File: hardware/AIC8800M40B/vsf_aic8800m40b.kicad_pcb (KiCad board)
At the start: 4 copper layers, 36.8 x 57.2 mm, 86 parts, among them J1 USB_A, J2 USB_C_Receptacle_USB2.0, J3 USB_C_Receptacle_USB2.0, J4 Micro_SD_Card_Det1, J6 Conn_Coaxial, J7 Conn_Coaxial, J8 Conn_02x15_Odd_Even, Q1 S9013, SW1 SW_Push, SW2 SW_Push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

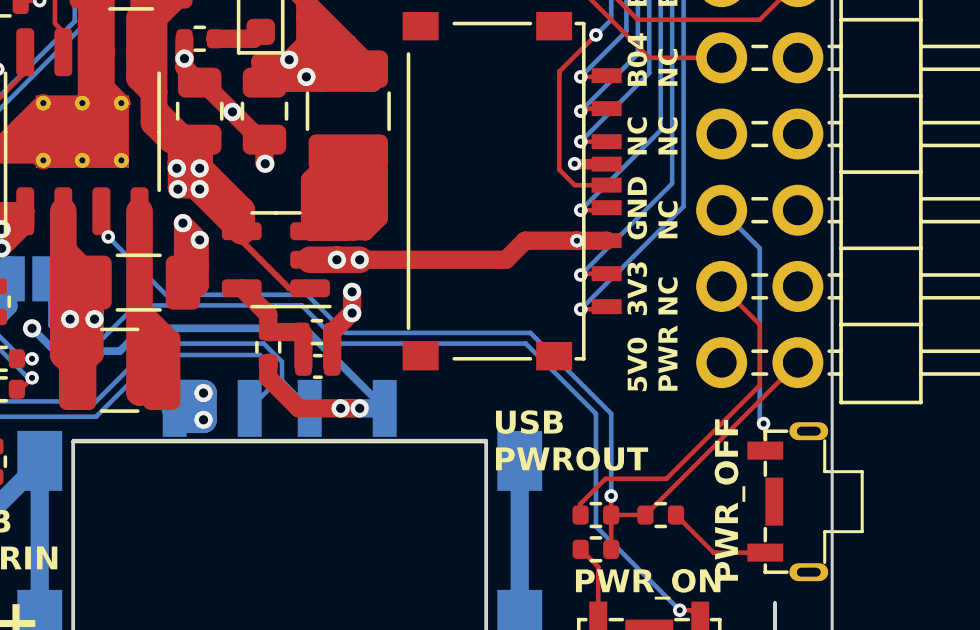
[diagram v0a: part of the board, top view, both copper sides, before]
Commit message: [hardware/aic8800m40b] connect usb signals to pin header
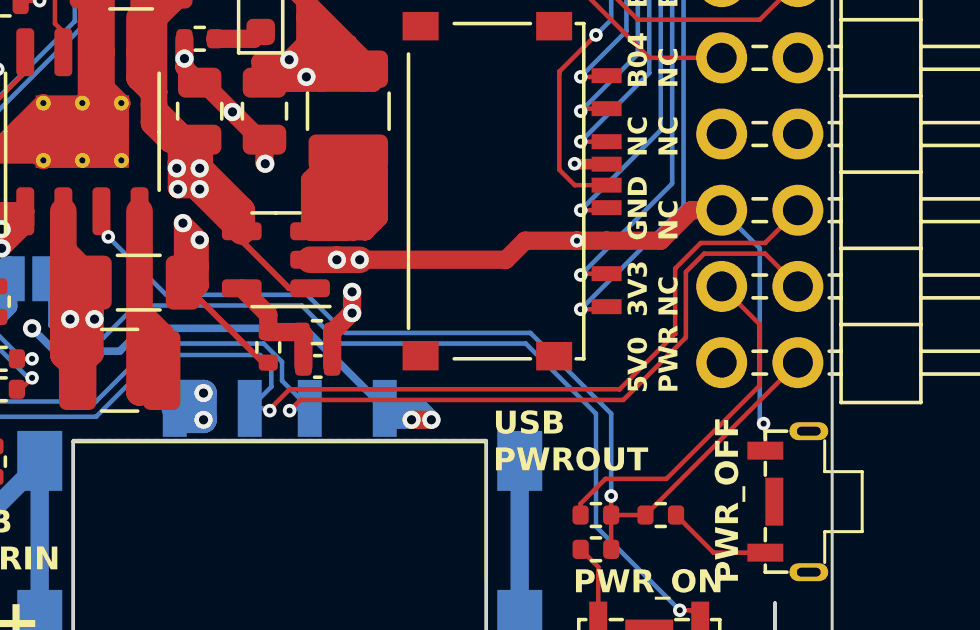
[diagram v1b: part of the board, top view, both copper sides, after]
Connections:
- J8 pad 26: unconnected-(J8-Pin_26-Pad26) -> /_USB_DM
- J8 pad 28: unconnected-(J8-Pin_28-Pad28) -> /_USB_DP
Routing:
- net /_USB_DM: track 18.3 -> 40.7 mm, vias 2 -> 3
- net /_USB_DP: track 18.2 -> 39.7 mm, vias 2 -> 3
- net GND: track 332.8 -> 342.2 mm

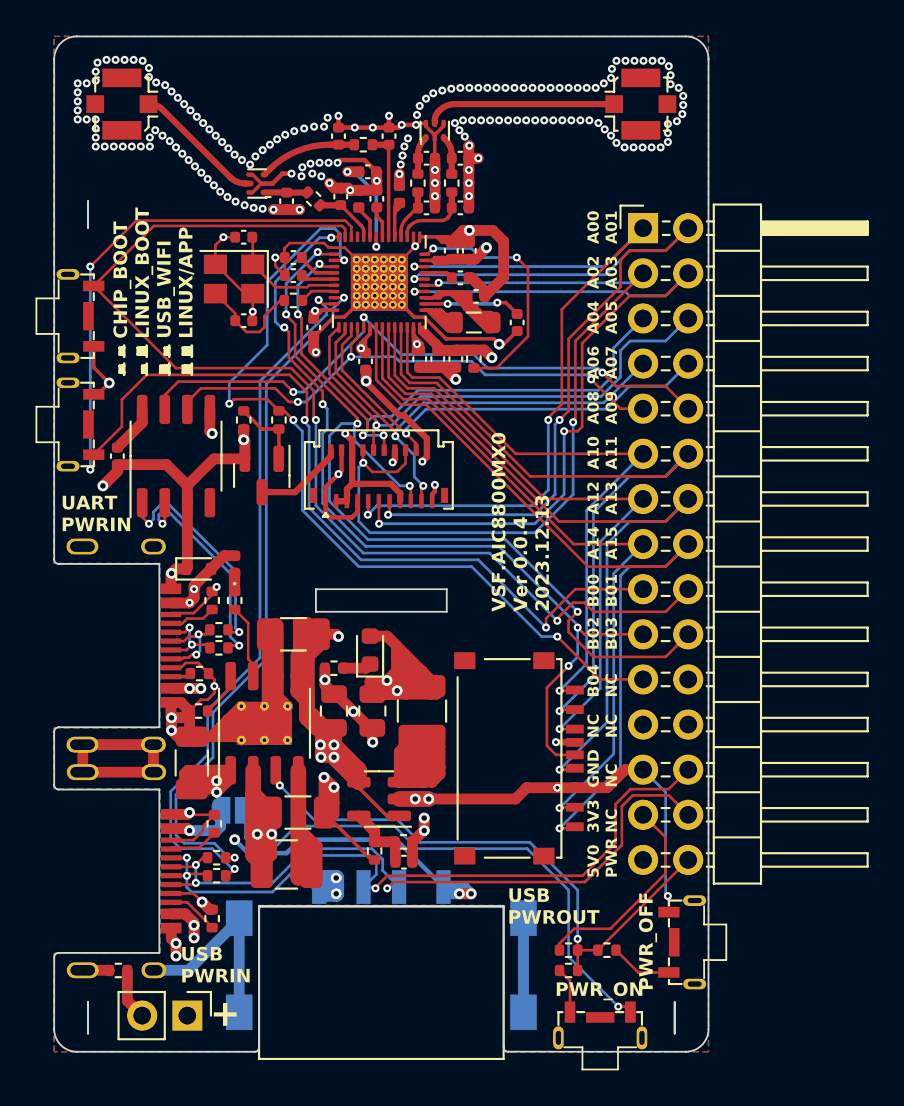
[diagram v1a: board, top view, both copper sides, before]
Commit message: [hardware/aic8800m40b] update silks
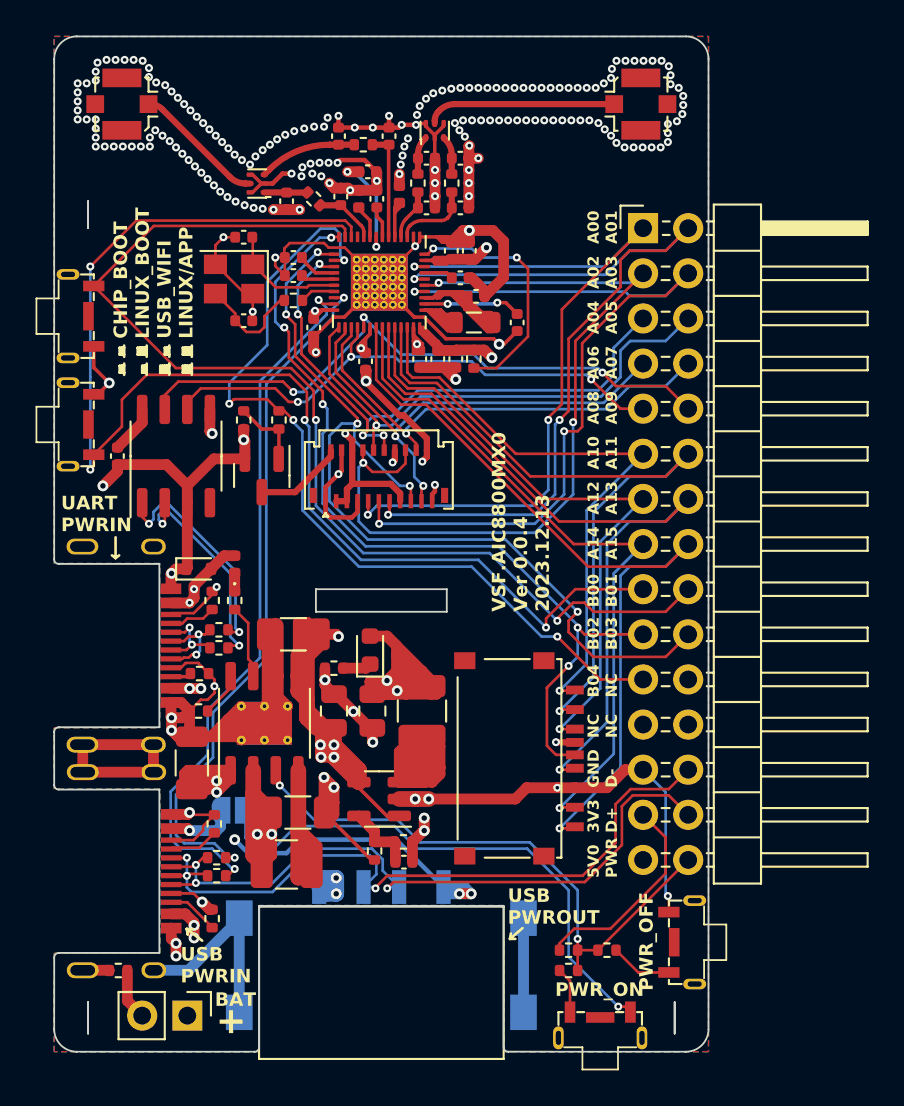
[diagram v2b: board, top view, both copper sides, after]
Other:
- board text added: "3V3 D+"
- board text added: "GND D-"
- board text removed: "3V3 NC"
- board text removed: "GND NC"
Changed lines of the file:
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@@
   (gr_line (start 206.883 112.776) (end 207.01 112.776)
     (stroke (width 0.15) (type default)) (layer "F.SilkS"))
+  (gr_line (start 211.5312 146.1516) (end 210.6676 145.4912)
+    (stroke (width 0.15) (type default)) (layer "F.SilkS"))
   (gr_line (start 209.169 114.173) (end 209.169 113.792)
     (stroke (width 0.15) (type default)) (layer "F.SilkS"))
@@
   (gr_line (start 208.407 113.157) (end 208.28 113.157)
     (stroke (width 0.15) (type default)) (layer "F.SilkS"))
+  (gr_line (start 210.6676 145.4912) (end 211.0232 145.4912)
+    (stroke (width 0.15) (type default)) (layer "F.SilkS"))
   (gr_line (start 208.28 113.792) (end 208.407 113.792)
     (stroke (width 0.15) (type default)) (layer "F.SilkS"))
@@
   (gr_line (start 210.566 112.776) (end 210.566 113.157)
     (stroke (width 0.15) (type default)) (layer "F.SilkS"))
+  (gr_line (start 210.7184 145.796) (end 210.6676 145.4912)
+    (stroke (width 0.15) (type default)) (layer "F.SilkS"))
   (gr_line (start 207.137 112.649) (end 207.137 113.284)
     (stroke (width 0.15) (type default)) (layer "F.SilkS"))
+  (gr_line (start 210.6676 145.4912) (end 210.7184 145.796)
+    (stroke (width 0.15) (type default)) (layer "F.SilkS"))
   (gr_line (start 207.899 112.776) (end 207.899 113.157)
     (stroke (width 0.15) (type default)) (layer "F.SilkS"))
@@
   (gr_line (start 210.566 113.792) (end 210.693 113.792)
     (stroke (width 0.15) (type default)) (layer "F.SilkS"))
+  (gr_line (start 206.6544 124.6124) (end 206.8576 124.46)
+    (stroke (width 0.15) (type default)) (layer "F.SilkS"))
   (gr_line (start 209.169 113.792) (end 209.296 113.792)
     (stroke (width 0.15) (type default)) (layer "F.SilkS"))
@@
   (gr_line (start 209.423 112.776) (end 209.55 112.776)
     (stroke (width 0.15) (type default)) (layer "F.SilkS"))
+  (gr_line (start 229.5652 145.4404) (end 228.854 146.05)
+    (stroke (width 0.15) (type default)) (layer "F.SilkS"))
   (gr_line (start 210.693 113.792) (end 210.693 114.173)
     (stroke (width 0.15) (type default)) (layer "F.SilkS"))
@@
   (gr_line (start 206.883 114.173) (end 207.01 114.173)
     (stroke (width 0.15) (type default)) (layer "F.SilkS"))
+  (gr_line (start 206.6544 124.6124) (end 206.4512 124.46)
+    (stroke (width 0.15) (type default)) (layer "F.SilkS"))
   (gr_line (start 207.01 113.792) (end 207.01 114.173)
     (stroke (width 0.15) (type default)) (layer "F.SilkS"))
@@
   (gr_line (start 209.423 114.173) (end 209.55 114.173)
     (stroke (width 0.15) (type default)) (layer "F.SilkS"))
+  (gr_line (start 228.854 146.05) (end 228.9048 145.7452)
+    (stroke (width 0.15) (type default)) (layer "F.SilkS"))
   (gr_line (start 209.55 113.792) (end 209.55 114.173)
     (stroke (width 0.15) (type default)) (layer "F.SilkS"))
@@
   (gr_line (start 207.137 113.665) (end 207.137 114.3)
     (stroke (width 0.15) (type default)) (layer "F.SilkS"))
+  (gr_line (start 228.854 146.05) (end 229.1588 146.05)
+    (stroke (width 0.15) (type default)) (layer "F.SilkS"))
   (gr_line (start 208.407 112.649) (end 208.407 113.284)
     (stroke (width 0.15) (type default)) (layer "F.SilkS"))
@@
     (stroke (width 0.15) (type default)) (layer "F.SilkS"))
   (gr_line (start 208.28 114.173) (end 208.28 113.792)
+    (stroke (width 0.15) (type default)) (layer "F.SilkS"))
+  (gr_line (start 206.6544 123.444) (end 206.6544 124.6124)
     (stroke (width 0.15) (type default)) (layer "F.SilkS"))
   (gr_line (start 209.55 113.792) (end 209.423 113.792)
@@
     (effects (font (size 0.762 0.762) (thickness 0.1524) bold) (justify left bottom))
   )
-  (gr_text "GND\nNC" (at 234.95 137.541 90) (layer "F.SilkS")
-    (effects (font (size 0.635 0.635) (thickness 0.1524) bold) (justify left bottom))
-  )
-  (gr_text "3V3\nNC" (at 234.95 140.081 90) (layer "F.SilkS")
+  (gr_text "GND\nD-" (at 234.95 137.541 90) (layer "F.SilkS")
+    (effects (font (size 0.635 0.635) (thickness 0.1524) bold) (justify left bottom))
+  )
+  (gr_text "3V3\nD+" (at 234.95 140.081 90) (layer "F.SilkS")
     (effects (font (size 0.635 0.635) (thickness 0.1524) bold) (justify left bottom))
   )
@@
     (effects (font (size 0.762 0.762) (thickness 0.1524) bold) (justify left bottom))
   )
-  (gr_text "+" (at 211.963 151.13) (layer "F.SilkS")
+  (gr_text "+" (at 212.2932 151.5364) (layer "F.SilkS")
     (effects (font (size 1.5 1.5) (thickness 0.3) bold) (justify left bottom))
   )
@@
     (effects (font (size 0.635 0.635) (thickness 0.1524) bold) (justify left bottom))
   )
+  (gr_text "BAT" (at 212.2424 149.9108) (layer "F.SilkS")
+    (effects (font (size 0.762 0.762) (thickness 0.1524) bold) (justify left bottom))
+  )
   (segment (start 219.86 103.909) (end 219.738 103.787) (width 0.6096) (layer "F.Cu") (net 1))
